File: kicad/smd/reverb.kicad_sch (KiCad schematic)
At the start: 28 parts, among them IC1 TL072CP

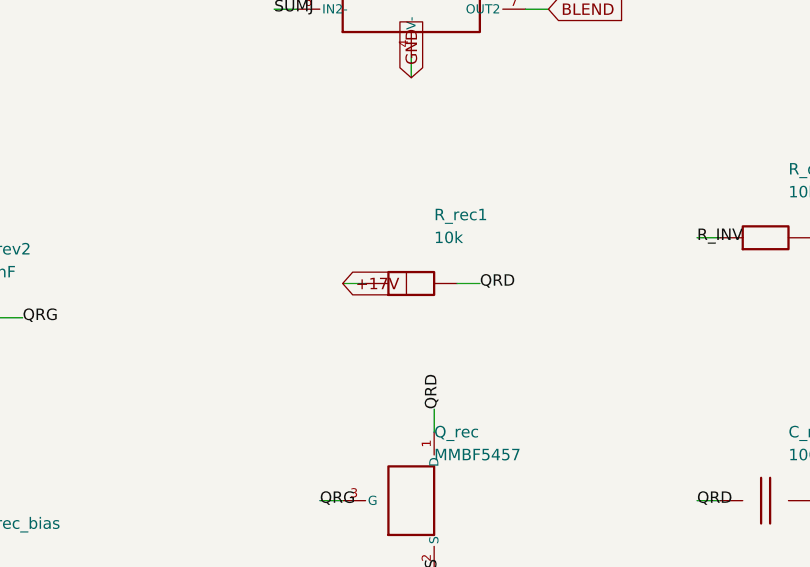
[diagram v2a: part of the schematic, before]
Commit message: Noise, hum, crosstalk and thermal models; three design fixes; JLCPCB rules and cost
New models (docs/06c, spice/): a .noise run of the whole front end including the
LM317's own rail noise, the rail-ripple paths to the speaker, a vactrol-level tremolo
depth model, an electro-thermal LM1875 ladder, and a geometric crosstalk audit of the
routed boards (kicad/gen/crosstalk_audit.py). They found three defects:

- Errata #21 (hum + hiss): the LM1875 bias divider had no bypass (+4 dB ripple to
  speaker, 0.4 Vrms of 100 Hz at idle) and the LM317's 0.5 mV of noise reached the
  0 dB-PSRR JFET stages (23 dB above their floor, SNR 34 dB). Fixed with C_bref +
  R_bias3 on the power amp, C_adj on the regulator, and an RC-decoupled +17V_PRE rail
  for Q1/Q2/Q_rec: hum 408 mV -> 0.3 mV, EIN 37 -> 2.7 uV, SNR 34 -> 57 dB.
- Errata #22 (tremolo depth 1.7 dB): the vactrol LED was returned to ground from a
  mid-rail LFO -> 7 mA DC, a fixed -20 dB pad. LED limiter (2 V swing, LED_rate is one
  limiter LED) + Q_trem 2N3904/MMBT3904 emitter follower AC-coupled from the depth
  pot -> 15 dB depth, 0.8 dB insertion loss.
- Errata #23 (fab): stock TO-92 and the LM1875 footprint were under JLCPCB's 0.18 mm
  annular-ring minimum -> TO-92_Inline_Wide and 1.5 mm LM1875 pads; both .kicad_pro
  carry JLC's 2-layer limits as DRC constraints. Cost: all SMD caps 1206 (basic
  library), "(opt)" MRB caps DNP, gyrator on E24 values (same 1.86 H): 7 -> 2
  extended part types, ~$32 -> ~$17 assembly for five boards (kicad/gen/jlc_cost.py);
  three fiducials on the SMD board.

Crosstalk -> two routing rules (.kicad_dru: HighCurrent 0.6/0.4 mm and TankDrive
1.2/0.8 mm from signal copper, THT/SMD) that route_board.py also hands the router as
class clearances; keepout rule areas along the edge and around the mounting holes.
Thermal: Part 5's <= 2.5 K/W heatsink confirmed with numbers (Tj 97 C at 40 C ambient,
worst-case sine; 8-10 K/W clip-ons reach shutdown).

Placer: short parts stack beside tall ones i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
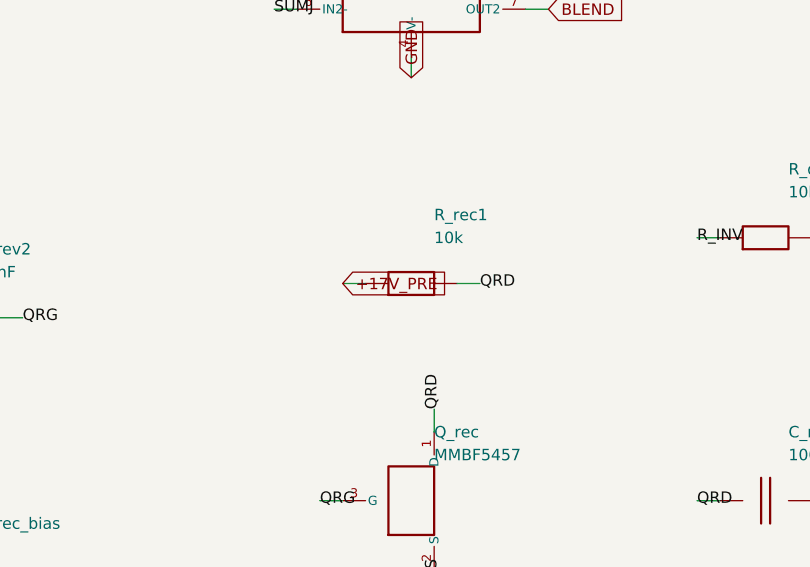
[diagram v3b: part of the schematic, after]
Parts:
- C_drymix, C_wetmix: footprint Capacitor_SMD:C_1210_3225Metric -> Capacitor_SMD:C_1206_3216Metric
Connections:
- net +17V: no longer R_rec1.1
- new net +17V_PRE: R_rec1.1

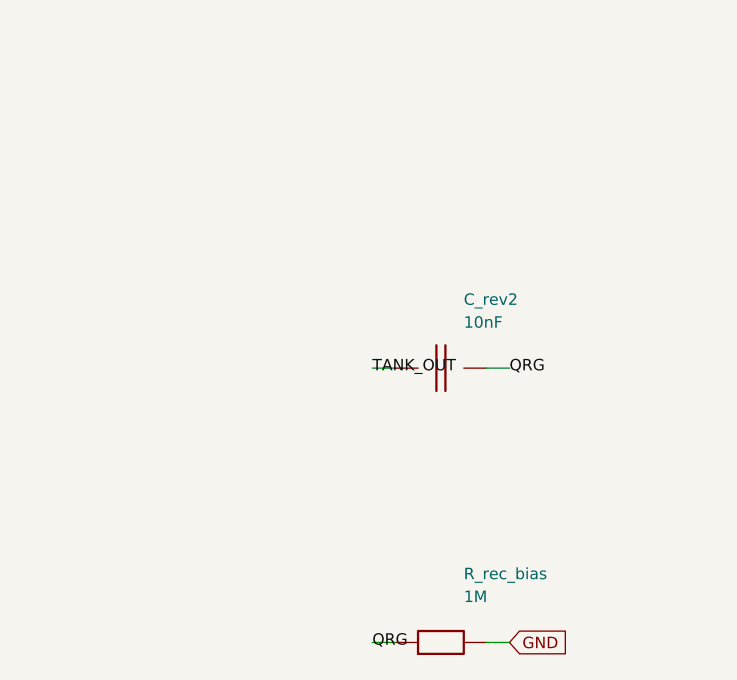
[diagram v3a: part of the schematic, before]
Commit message: Four-layer boards, no routes through footprints, rules by impedance, RF stoppers
Both boards move to a 4-layer stack (JLC04161H-7628): F.Cu signal, In1 solid GND
plane, In2 inner signal layer, B.Cu signal + shield-only GND pour, locked perimeter
GND stitching vias every 15 mm. Outer traces sit 0.21 mm from the plane instead of
1.5 mm; the long runs live on In2 under the plane and the outer layers carry escapes.

- No routes through footprints: gen_pcb writes keepout rule areas (kp_<ref>, tracks;
  vias too under SMD parts; component side) between every part's pads -- pin-to-pin
  strips and the body between rows -- with same-net pin gaps exempt and power-only
  parts exempt. 155 / 147 areas. Freerouting gets them as keepouts, KiCad DRC checks.
- Rules by impedance: new HiZ net class (0.3 mm; gates, RF nodes, tone ladder and
  wipers, LFO timing, MRB tank, PA + input), Default = low-Z signal, Power 1.0 mm,
  HighCurrent 1.5 mm, TankDrive; .kicad_dru: HighCurrent >= 0.6 mm from any signal
  trace, tank drive >= 0.8 mm from the return (SMD 0.4 / 0.6), tracks and vias only;
  route_board hands the router the same per-class clearances.
- RF stoppers R_rf1/C_rf1 (1k + 100 pF) at Q1's gate and R_rf2/C_rf2 at the recovery
  JFET's gate (the guitar and tank cables are the antennas). Noise floor unchanged.
- route_board: strips the plane layer from the DSN (Freerouting 1.9 ignores
  (active off) and routed 7 m of copper on the planes; typed as a power layer it
  treated every through-hole pad as connected), routes inner signal layers, per-board
  class clearances, 4-layer defaults.
- SMD board 170x100 mm, 1.2 mm gap (was 155x90 / 0.5): with the keepouts every SMD
  ground / rail pad needs a via beside it and none fitted; smaller SMD rail vias.
  THT gap 1.6 mm. Placer: gaps are the routing channels now.
- Crosstalk audit knows the 4-layer geometry; cost model notes the 4-layer PCB.

Routing: THT 218/226, 0 DRC errors, 0 rule hits; SMD 216/226, 1 starved thermal.
Crosstalk aft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
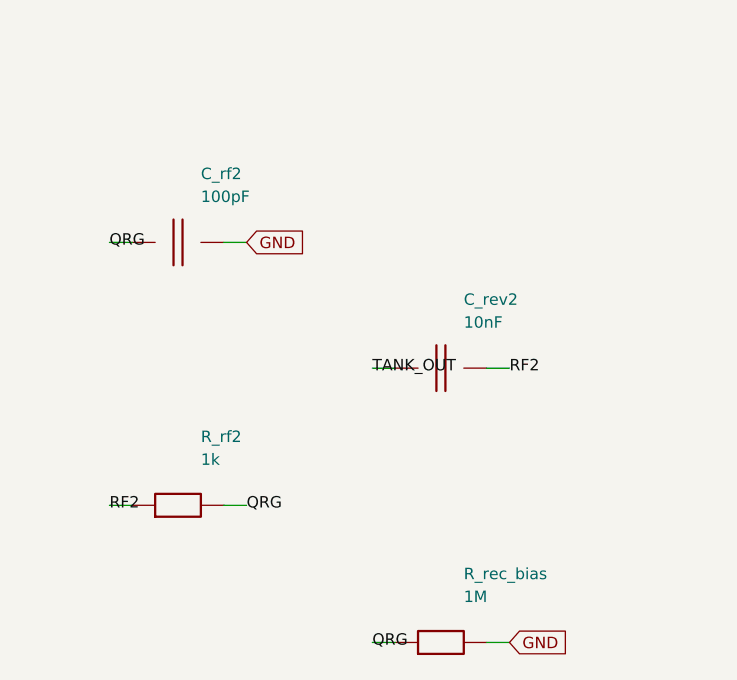
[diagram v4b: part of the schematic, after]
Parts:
- added C_rf2: 100pF, Capacitor_SMD:C_1206_3216Metric, symbol cr_primitives:C
- added R_rf2: 1k, Resistor_SMD:R_0805_2012Metric, symbol cr_primitives:R
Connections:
- net GND: now also C_rf2.2
- net QRG: now also C_rf2.1, R_rf2.2; no longer C_rev2.2
- new net RF2: C_rev2.2, R_rf2.1
